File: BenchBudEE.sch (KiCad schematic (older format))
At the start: 0 parts

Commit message: Completed -Defining IO Video
http://contextualelectronics.com/module-2/defining-your-inputs-and-outputs/
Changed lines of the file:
@@
 $EndDescr
 $Sheet
-S 3200 4900 1400 950
+S 2500 4400 1400 2650
 U 52EEE583
 F0 "Arduino" 50
 F1 "Arduino.sch" 50
+F2 "Relay+" O R 3900 6700 60
+F3 "Relay-" I R 3900 6800 60
+F4 "MOSI" O R 3900 6150 60
+F5 "MISO" I R 3900 6250 60
+F6 "SCLK" O R 3900 6350 60
+F7 "CS_N" O R 3900 6450 60
+F8 "LED_EN" O R 3900 5700 60
+F9 "LED_FREQ" O R 3900 5800 60
+F10 "FAN_EN" O R 3900 5250 60
+F11 "TACH_MEAS" I R 3900 5350 60
 $EndSheet
 $Sheet
-S 8000 1950 1400 950
+S 8000 4350 1400 950
 U 52EEE626
 F0 "Thermocouple" 50
 F1 "Thermocouple.sch" 50
-F2 "TC IN +" I R 9400 2200 60
-F3 "TC IN -" I R 9400 2350 60
+F2 "TC IN +" I R 9400 4600 60
+F3 "TC IN -" I R 9400 4750 60
+F4 "MOSI" I L 8000 4500 60
+F5 "MISO" O L 8000 4650 60
+F6 "SCLK" I L 8000 4800 60
+F7 "CS_N" I L 8000 4950 60
 $EndSheet
 $Sheet
-S 8000 5700 1400 1000
+S 8000 5600 1400 1000
 U 52EEE642
 F0 "Relay" 50
 F1 "Relay.sch" 50
+F2 "DIN+" I L 8000 5800 60
+F3 "DIN-" O L 8000 6000 60
+F4 "Relay+" I R 9400 5800 60
+F5 "Relay-" O R 9400 6000 60
 $EndSheet
 $Sheet
-S 3200 2850 1400 950
+S 2500 2850 1400 950
 U 52EEE692
 F0 "Power" 50
@@
 $EndSheet
 $Sheet
-S 8000 4450 1400 950
+S 8000 3050 1400 950
 U 52EEE6FA
 F0 "LED_Driver" 50
 F1 "LED_Driver.sch" 50
+F2 "EN" I L 8000 3200 60
+F3 "FREQ" I L 8000 3350 60
+F4 "String+" O R 9400 3200 60
+F5 "String-" I R 9400 3350 60
 $EndSheet
 $Sheet
-S 8000 3150 1400 1000
+S 8000 1750 1400 1000
 U 52EEE752
 F0 "Fan" 50
 F1 "Fan.sch" 50
+F2 "Power+" O R 9400 1900 60
+F3 "Power-" I R 9400 2050 60
+F4 "Tach" I R 9400 2200 60
+F5 "Tach_Out" O L 8000 2200 60
+F6 "Fan_In" I L 8000 1900 60
 $EndSheet
 $Sheet

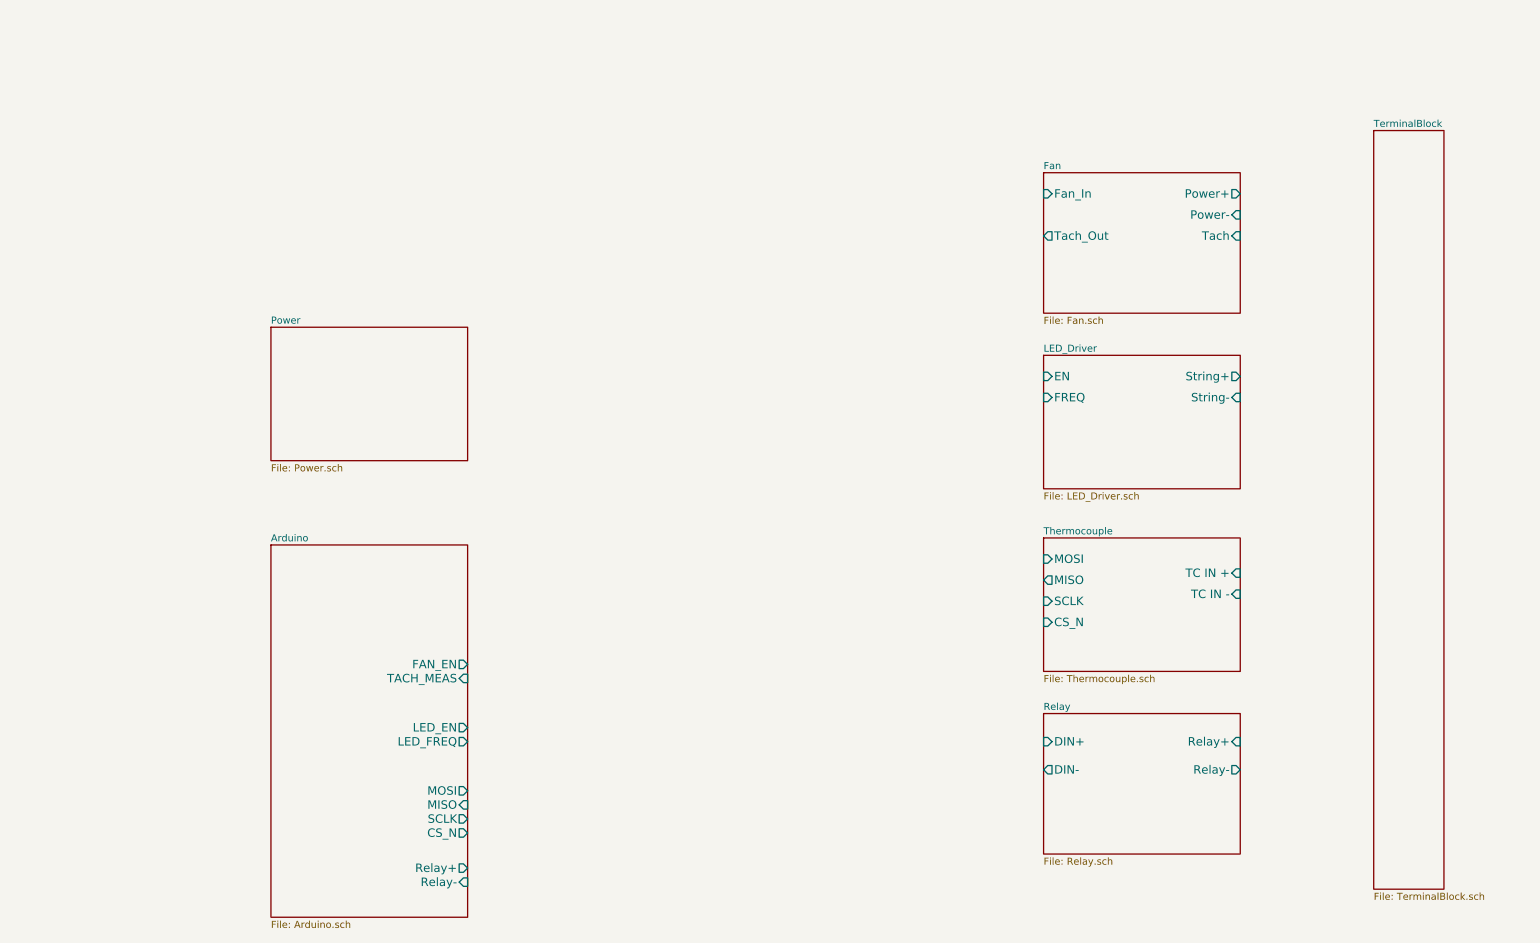
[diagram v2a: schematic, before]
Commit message: Completed LED Driver Video + Power Module
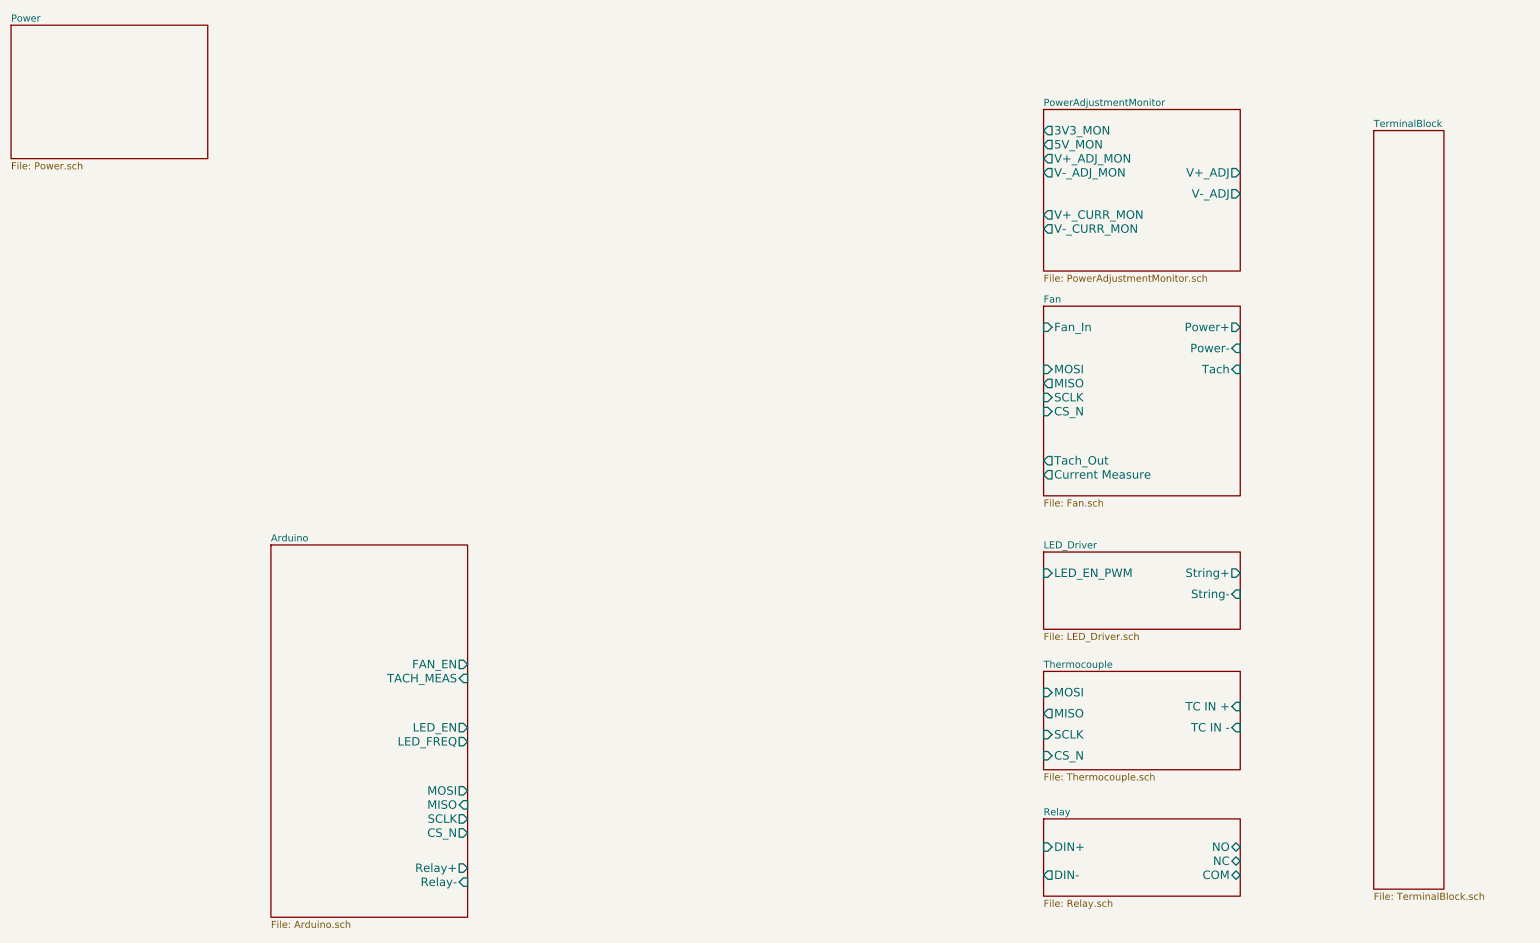
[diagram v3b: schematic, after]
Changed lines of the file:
@@
 LIBS:contrib
 LIBS:valves
+LIBS:BenchBudEE_Parts
 LIBS:BenchBudEE-cache
 EELAYER 27 0
@@
 $Descr A4 11693 8268
 encoding utf-8
-Sheet 1 8
+Sheet 1 9
 Title ""
-Date "6 feb 2014"
+Date "10 feb 2014"
 Rev ""
 Comp ""
@@
 $EndSheet
 $Sheet
-S 8000 4350 1400 950
+S 8000 5300 1400 700
 U 52EEE626
 F0 "Thermocouple" 50
 F1 "Thermocouple.sch" 50
-F2 "TC IN +" I R 9400 4600 60
-F3 "TC IN -" I R 9400 4750 60
-F4 "MOSI" I L 8000 4500 60
-F5 "MISO" O L 8000 4650 60
-F6 "SCLK" I L 8000 4800 60
-F7 "CS_N" I L 8000 4950 60
+F2 "TC IN +" I R 9400 5550 60
+F3 "TC IN -" I R 9400 5700 60
+F4 "MOSI" I L 8000 5450 60
+F5 "MISO" O L 8000 5600 60
+F6 "SCLK" I L 8000 5750 60
+F7 "CS_N" I L 8000 5900 60
 $EndSheet
 $Sheet
-S 8000 5600 1400 1000
-U 52EEE642
-F0 "Relay" 50
-F1 "Relay.sch" 50
-F2 "DIN+" I L 8000 5800 60
-F3 "DIN-" O L 8000 6000 60
-F4 "Relay+" I R 9400 5800 60
-F5 "Relay-" O R 9400 6000 60
-$EndSheet
-$Sheet
-S 2500 2850 1400 950
+S 650  700  1400 950
 U 52EEE692
 F0 "Power" 50
@@
 $EndSheet
 $Sheet
-S 8000 3050 1400 950
+S 8000 4450 1400 550
 U 52EEE6FA
 F0 "LED_Driver" 50
 F1 "LED_Driver.sch" 50
-F2 "EN" I L 8000 3200 60
-F3 "FREQ" I L 8000 3350 60
-F4 "String+" O R 9400 3200 60
-F5 "String-" I R 9400 3350 60
+F2 "String+" O R 9400 4600 60
+F3 "String-" I R 9400 4750 60
+F4 "LED_EN_PWM" I L 8000 4600 60
 $EndSheet
 $Sheet
-S 8000 1750 1400 1000
+S 8000 2700 1400 1350
 U 52EEE752
 F0 "Fan" 50
 F1 "Fan.sch" 50
-F2 "Power+" O R 9400 1900 60
-F3 "Power-" I R 9400 2050 60
-F4 "Tach" I R 9400 2200 60
-F5 "Tach_Out" O L 8000 2200 60
-F6 "Fan_In" I L 8000 1900 60
+F2 "Power+" O R 9400 2850 60
+F3 "Power-" I R 9400 3000 60
+F4 "Tach" I R 9400 3150 60
+F5 "Tach_Out" O L 8000 3800 60
+F6 "Fan_In" I L 8000 2850 60
+F7 "Current Measure" O L 8000 3900 60
+F8 "MOSI" I L 8000 3150 60
+F9 "MISO" O L 8000 3250 60
+F10 "SCLK" I L 8000 3350 60
+F11 "CS_N" I L 8000 3450 60
 $EndSheet
 $Sheet
@@
 F1 "TerminalBlock.sch" 50
 $EndSheet
+$Sheet
+S 8000 6350 1400 550
+U 52EEE642
+F0 "Relay" 50
+F1 "Relay.sch" 50
+F2 "DIN+" I L 8000 6550 60
+F3 "DIN-" O L 8000 6750 60
+F4 "NO" B R 9400 6550 60
+F5 "NC" B R 9400 6650 60
+F6 "COM" B R 9400 6750 60
+$EndSheet
+$Sheet
+S 8000 1300 1400 1150
+U 52F6797D
+F0 "PowerAdjustmentMonitor" 50
+F1 "PowerAdjustmentMonitor.sch" 50
+F2 "V+_ADJ" O R 9400 1750 60
+F3 "V-_ADJ" O R 9400 1900 60
+F4 "3V3_MON" O L 8000 1450 60
+F5 "5V_MON" O L 8000 1550 60
+F6 "V+_ADJ_MON" O L 8000 1650 60
+F7 "V-_ADJ_MON" O L 8000 1750 60
+F8 "V+_CURR_MON" O L 8000 2050 60
+F9 "V-_CURR_MON" O L 8000 2150 60
+$EndSheet
 $EndSCHEMATC

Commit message: Completed Arduino Module Video
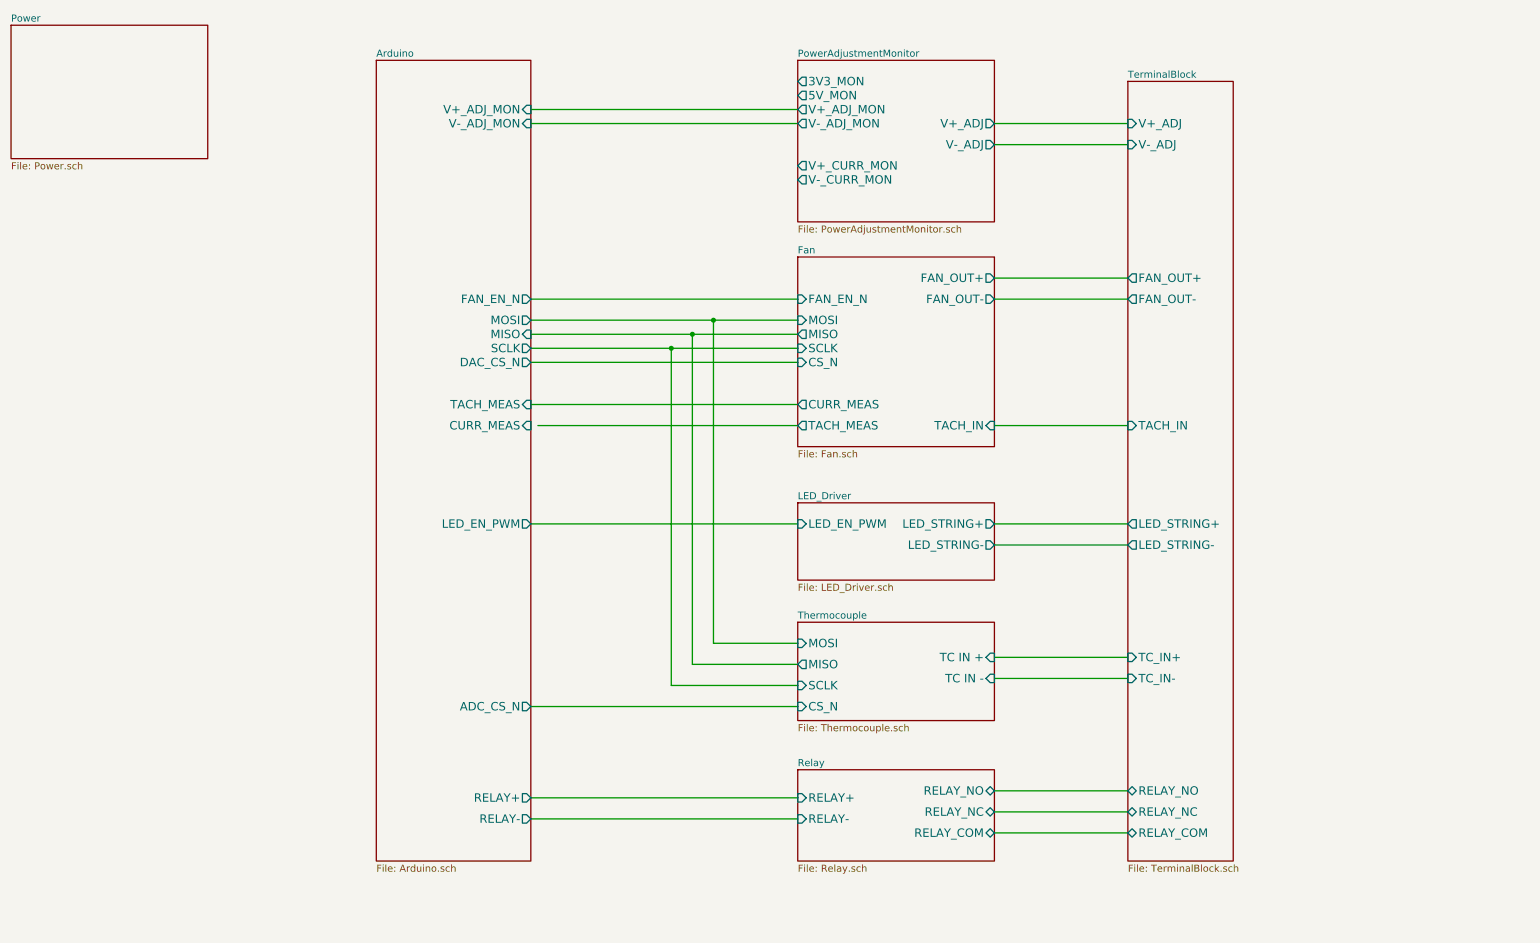
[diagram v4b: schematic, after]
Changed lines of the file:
@@
 Sheet 1 9
 Title ""
-Date "10 feb 2014"
+Date "11 feb 2014"
 Rev ""
 Comp ""
@@
 $EndDescr
 $Sheet
-S 2500 4400 1400 2650
+S 3250 950  1100 5700
 U 52EEE583
 F0 "Arduino" 50
 F1 "Arduino.sch" 50
-F2 "Relay+" O R 3900 6700 60
-F3 "Relay-" I R 3900 6800 60
-F4 "MOSI" O R 3900 6150 60
-F5 "MISO" I R 3900 6250 60
-F6 "SCLK" O R 3900 6350 60
-F7 "CS_N" O R 3900 6450 60
-F8 "LED_EN" O R 3900 5700 60
-F9 "LED_FREQ" O R 3900 5800 60
-F10 "FAN_EN" O R 3900 5250 60
-F11 "TACH_MEAS" I R 3900 5350 60
+F2 "MOSI" O R 4350 2800 60
+F3 "MISO" I R 4350 2900 60
+F4 "SCLK" O R 4350 3000 60
+F6 "TACH_MEAS" I R 4350 3400 60
+F7 "RELAY+" O R 4350 6200 60
+F8 "RELAY-" O R 4350 6350 60
+F9 "FAN_EN_N" O R 4350 2650 60
+F10 "CURR_MEAS" I R 4350 3550 60
+F11 "V+_ADJ_MON" I R 4350 1300 60
+F12 "V-_ADJ_MON" I R 4350 1400 60
+F13 "LED_EN_PWM" O R 4350 4250 60
+F14 "DAC_CS_N" O R 4350 3100 60
+F16 "ADC_CS_N" O R 4350 5550 60
 $EndSheet
 $Sheet
-S 8000 5300 1400 700
+S 6250 4950 1400 700
 U 52EEE626
 F0 "Thermocouple" 50
 F1 "Thermocouple.sch" 50
-F2 "TC IN +" I R 9400 5550 60
-F3 "TC IN -" I R 9400 5700 60
-F4 "MOSI" I L 8000 5450 60
-F5 "MISO" O L 8000 5600 60
-F6 "SCLK" I L 8000 5750 60
-F7 "CS_N" I L 8000 5900 60
+F2 "TC IN +" I R 7650 5200 60
+F3 "TC IN -" I R 7650 5350 60
+F4 "MOSI" I L 6250 5100 60
+F5 "MISO" O L 6250 5250 60
+F6 "SCLK" I L 6250 5400 60
+F7 "CS_N" I L 6250 5550 60
 $EndSheet
 $Sheet
@@
 $EndSheet
 $Sheet
-S 8000 4450 1400 550
+S 6250 4100 1400 550
 U 52EEE6FA
 F0 "LED_Driver" 50
 F1 "LED_Driver.sch" 50
-F2 "String+" O R 9400 4600 60
-F3 "String-" I R 9400 4750 60
-F4 "LED_EN_PWM" I L 8000 4600 60
+F2 "LED_EN_PWM" I L 6250 4250 60
+F3 "LED_STRING+" O R 7650 4250 60
+F4 "LED_STRING-" O R 7650 4400 60
 $EndSheet
 $Sheet
-S 8000 2700 1400 1350
+S 6250 6000 1400 650
+U 52EEE642
+F0 "Relay" 50
+F1 "Relay.sch" 50
+F2 "RELAY_NO" B R 7650 6150 60
+F3 "RELAY_NC" B R 7650 6300 60
+F4 "RELAY_COM" B R 7650 6450 60
+F5 "RELAY+" I L 6250 6200 60
+F6 "RELAY-" I L 6250 6350 60
+$EndSheet
+$Sheet
+S 6250 950  1400 1150
+U 52F6797D
+F0 "PowerAdjustmentMonitor" 50
+F1 "PowerAdjustmentMonitor.sch" 50
+F2 "V+_ADJ" O R 7650 1400 60
+F3 "V-_ADJ" O R 7650 1550 60
+F4 "3V3_MON" O L 6250 1100 60
+F5 "5V_MON" O L 6250 1200 60
+F6 "V+_ADJ_MON" O L 6250 1300 60
+F7 "V-_ADJ_MON" O L 6250 1400 60
+F8 "V+_CURR_MON" O L 6250 1700 60
+F9 "V-_CURR_MON" O L 6250 1800 60
+$EndSheet
+$Sheet
+S 6250 2350 1400 1350
 U 52EEE752
 F0 "Fan" 50
 F1 "Fan.sch" 50
-F2 "Power+" O R 9400 2850 60
-F3 "Power-" I R 9400 3000 60
-F4 "Tach" I R 9400 3150 60
-F5 "Tach_Out" O L 8000 3800 60
-F6 "Fan_In" I L 8000 2850 60
-F7 "Current Measure" O L 8000 3900 60
-F8 "MOSI" I L 8000 3150 60
-F9 "MISO" O L 8000 3250 60
-F10 "SCLK" I L 8000 3350 60
-F11 "CS_N" I L 8000 3450 60
+F2 "MOSI" I L 6250 2800 60
+F3 "MISO" O L 6250 2900 60
+F4 "SCLK" I L 6250 3000 60
+F5 "CS_N" I L 6250 3100 60
+F6 "FAN_OUT+" O R 7650 2500 60
+F7 "TACH_IN" I R 7650 3550 60
+F8 "TACH_MEAS" O L 6250 3550 60
+F9 "FAN_EN_N" I L 6250 2650 60
+F10 "CURR_MEAS" O L 6250 3400 60
+F11 "FAN_OUT-" O R 7650 2650 60
 $EndSheet
+Wire Wire Line
+	7650 6150 8600 6150
+Wire Wire Line
+	7650 6300 8600 6300
+Wire Wire Line
+	7650 6450 8600 6450
+Wire Wire Line
+	7650 5350 8600 5350
+Wire Wire Line
+	7650 5200 8600 5200
+Wire Wire Line
+	7650 4400 8600 4400
+Wire Wire Line
+	7650 4250 8600 4250
+Wire Wire Line
+	7650 3550 8600 3550
+Wire Wire Line
+	7650 2650 8600 2650
+Wire Wire Line
+	7650 2500 8600 2500
+Wire Wire Line
+	7650 1550 8600 1550
+Wire Wire Line
+	7650 1400 8600 1400
 $Sheet
-S 10350 1450 500  5400
+S 8600 1100 750  5550
 U 52EEE774
 F0 "TerminalBlock" 50
 F1 "TerminalBlock.sch" 50
+F2 "V+_ADJ" I L 8600 1400 60
+F3 "V-_ADJ" I L 8600 1550 60
+F4 "FAN_OUT+" O L 8600 2500 60
+F5 "FAN_OUT-" O L 8600 2650 60
+F6 "TACH_IN" I L 8600 3550 60
+F7 "LED_STRING+" O L 8600 4250 60
+F8 "LED_STRING-" O L 8600 4400 60
+F9 "TC_IN+" I L 8600 5200 60
+F10 "TC_IN-" I L 8600 5350 60
+F11 "RELAY_COM" B L 8600 6450 60
+F12 "RELAY_NC" B L 8600 6300 60
+F13 "RELAY_NO" B L 8600 6150 60
 $EndSheet
-$Sheet
-S 8000 6350 1400 550
-U 52EEE642
-F0 "Relay" 50
-F1 "Relay.sch" 50
-F2 "DIN+" I L 8000 6550 60
-F3 "DIN-" O L 8000 6750 60
-F4 "NO" B R 9400 6550 60
-F5 "NC" B R 9400 6650 60
-F6 "COM" B R 9400 6750 60
-$EndSheet
-$Sheet
-S 8000 1300 1400 1150
-U 52F6797D
-F0 "PowerAdjustmentMonitor" 50
-F1 "PowerAdjustmentMonitor.sch" 50
-F2 "V+_ADJ" O R 9400 1750 60
-F3 "V-_ADJ" O R 9400 1900 60
-F4 "3V3_MON" O L 8000 1450 60
-F5 "5V_MON" O L 8000 1550 60
-F6 "V+_ADJ_MON" O L 8000 1650 60
-F7 "V-_ADJ_MON" O L 8000 1750 60
-F8 "V+_CURR_MON" O L 8000 2050 60
-F9 "V-_CURR_MON" O L 8000 2150 60
-$EndSheet
+Wire Wire Line
+	4350 6350 6250 6350
+Wire Wire Line
+	4350 6200 6250 6200
+Wire Wire Line
+	4350 3100 6250 3100
+Wire Wire Line
+	4350 3000 6250 3000
+Wire Wire Line
+	4350 2900 6250 2900
+Wire Wire Line
+	4350 2800 6250 2800
+Wire Wire Line
+	4350 2650 6250 2650
+Wire Wire Line
+	4350 4250 6250 4250
+Wire Wire Line
+	4350 1300 6250 1300
+Wire Wire Line
+	4350 1400 6250 1400
+Wire Wire Line
+	6250 5100 5650 5100
+Wire Wire Line
+	5650 5100 5650 2800
+Connection ~ 5650 2800
+Wire Wire Line
+	6250 5250 5500 5250
+Wire Wire Line
+	5500 5250 5500 2900
+Connection ~ 5500 2900
+Wire Wire Line
+	6250 5400 5350 5400
+Wire Wire Line
+	5350 5400 5350 3000
+Connection ~ 5350 3000
+Wire Wire Line
+	4400 3550 6250 3550
+Wire Wire Line
+	4350 3400 6250 3400
+Wire Wire Line
+	4350 5550 6250 5550
 $EndSCHEMATC

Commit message: Fan Module Update
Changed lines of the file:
@@
 F3 "MISO" I R 4350 2900 60
 F4 "SCLK" O R 4350 3000 60
-F6 "TACH_MEAS" I R 4350 3400 60
-F7 "RELAY+" O R 4350 6200 60
-F8 "RELAY-" O R 4350 6350 60
-F9 "FAN_EN_N" O R 4350 2650 60
-F10 "CURR_MEAS" I R 4350 3550 60
-F11 "V+_ADJ_MON" I R 4350 1300 60
-F12 "V-_ADJ_MON" I R 4350 1400 60
-F13 "LED_EN_PWM" O R 4350 4250 60
-F14 "DAC_CS_N" O R 4350 3100 60
-F16 "ADC_CS_N" O R 4350 5550 60
+F5 "TACH_MEAS" I R 4350 3400 60
+F6 "RELAY+" O R 4350 6200 60
+F7 "RELAY-" O R 4350 6350 60
+F8 "CURR_MEAS" I R 4350 3550 60
+F9 "V+_ADJ_MON" I R 4350 1300 60
+F10 "V-_ADJ_MON" I R 4350 1400 60
+F11 "LED_EN_PWM" O R 4350 4250 60
+F12 "DAC_CS_N" O R 4350 3100 60
+F13 "ADC_CS_N" O R 4350 5550 60
+F14 "FAN_PWM" O R 4350 2650 60
 $EndSheet
 $Sheet
@@
 F7 "TACH_IN" I R 7650 3550 60
 F8 "TACH_MEAS" O L 6250 3550 60
-F9 "FAN_EN_N" I L 6250 2650 60
-F10 "CURR_MEAS" O L 6250 3400 60
-F11 "FAN_OUT-" O R 7650 2650 60
+F9 "CURR_MEAS" O L 6250 3400 60
+F10 "FAN_OUT-" O R 7650 2650 60
+F11 "FAN_PWM" I L 6250 2650 60
+F12 "FAN_MODE" I L 6250 2500 60
 $EndSheet
 Wire Wire Line

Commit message: Started Layout Outline.  Completed other schem videos
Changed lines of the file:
@@
 Sheet 1 9
 Title ""
-Date "11 feb 2014"
+Date "17 feb 2014"
 Rev ""
 Comp ""
@@
 Comment4 ""
 $EndDescr
-$Sheet
-S 3250 950  1100 5700
-U 52EEE583
-F0 "Arduino" 50
-F1 "Arduino.sch" 50
-F2 "MOSI" O R 4350 2800 60
-F3 "MISO" I R 4350 2900 60
-F4 "SCLK" O R 4350 3000 60
-F5 "TACH_MEAS" I R 4350 3400 60
-F6 "RELAY+" O R 4350 6200 60
-F7 "RELAY-" O R 4350 6350 60
-F8 "CURR_MEAS" I R 4350 3550 60
-F9 "V+_ADJ_MON" I R 4350 1300 60
-F10 "V-_ADJ_MON" I R 4350 1400 60
-F11 "LED_EN_PWM" O R 4350 4250 60
-F12 "DAC_CS_N" O R 4350 3100 60
-F13 "ADC_CS_N" O R 4350 5550 60
-F14 "FAN_PWM" O R 4350 2650 60
-$EndSheet
 $Sheet
 S 6250 4950 1400 700
@@
 F6 "V+_ADJ_MON" O L 6250 1300 60
 F7 "V-_ADJ_MON" O L 6250 1400 60
-F8 "V+_CURR_MON" O L 6250 1700 60
-F9 "V-_CURR_MON" O L 6250 1800 60
 $EndSheet
 $Sheet
@@
 Wire Wire Line
 	4350 5550 6250 5550
+$Sheet
+S 3250 950  1100 5700
+U 52EEE583
+F0 "Arduino" 50
+F1 "Arduino.sch" 50
+F2 "MOSI" O R 4350 2800 60
+F3 "MISO" I R 4350 2900 60
+F4 "SCLK" O R 4350 3000 60
+F5 "TACH_MEAS" I R 4350 3400 60
+F6 "RELAY+" O R 4350 6200 60
+F7 "RELAY-" O R 4350 6350 60
+F8 "CURR_MEAS" I R 4350 3550 60
+F9 "V+_ADJ_MON" I R 4350 1300 60
+F10 "V-_ADJ_MON" I R 4350 1400 60
+F11 "LED_EN_PWM" O R 4350 4250 60
+F12 "DAC_CS_N" O R 4350 3100 60
+F13 "ADC_CS_N" O R 4350 5550 60
+F14 "FAN_PWM" O R 4350 2650 60
+$EndSheet
 $EndSCHEMATC
